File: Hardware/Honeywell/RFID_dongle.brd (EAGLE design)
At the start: 100 x 80 mm, 11 parts, among them J1 USB_B_PTH, J2 USB_A_PTH_MALE, J5 1X2-3.5MM, J6 1X2-3.5MM, Q1 35A/25V/8.5mΩ

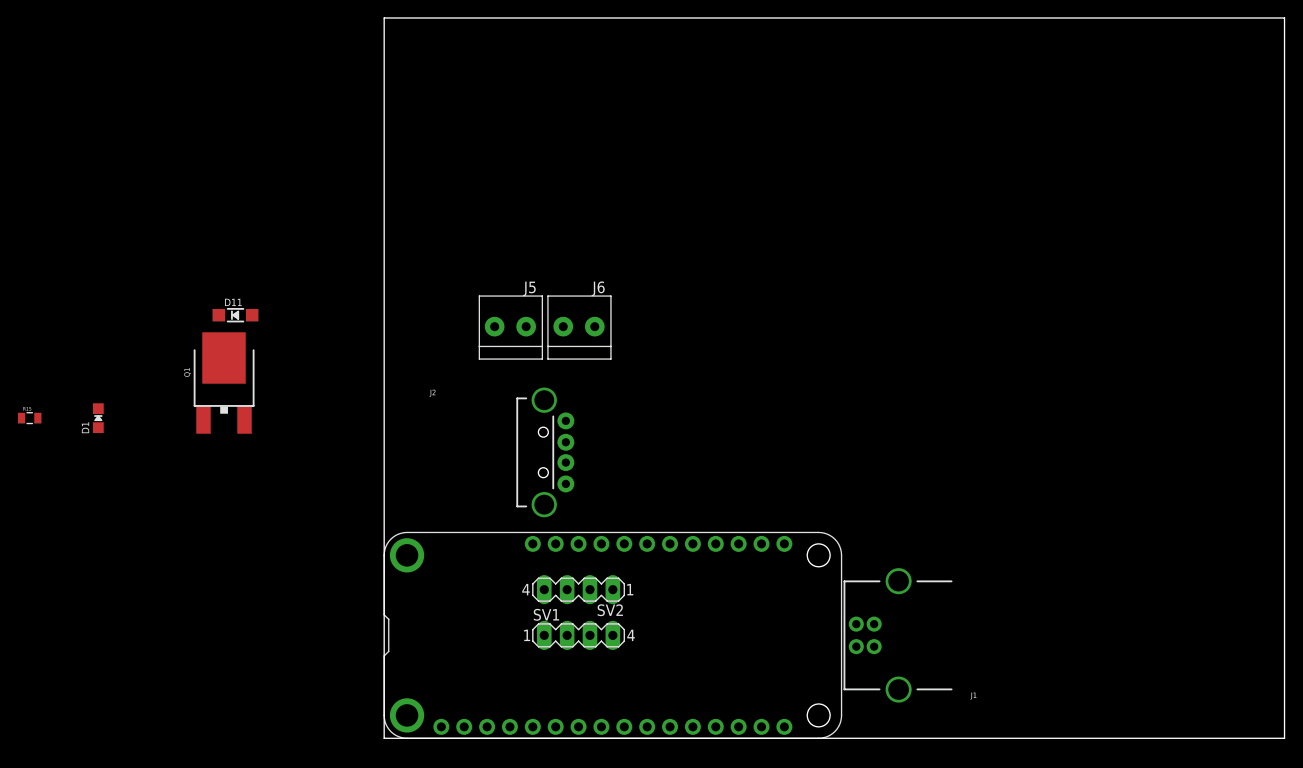
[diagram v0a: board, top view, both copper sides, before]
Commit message: HEEP-878 WIP, to be converted to USB switch IC
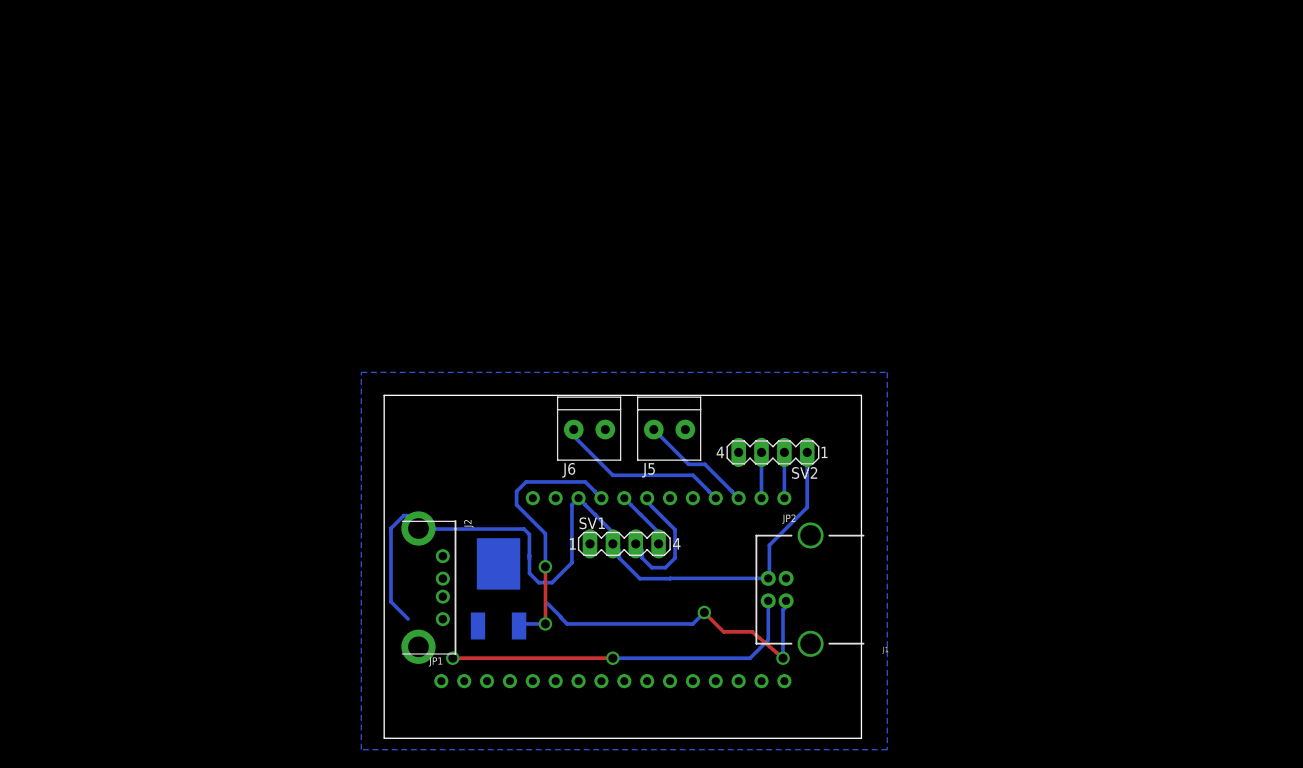
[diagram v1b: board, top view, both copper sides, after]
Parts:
- removed D1: (no value), microbuilder:CHIPLED_0805_NOOUTLINE
- removed D11: (no value), microbuilder:SOD-123
- removed MS1: FEATHERWING_NODIM, adafruit:FEATHERWING_DIM
- removed R15: 1K, SparkFun-Passives:0805
- added JP1: (no value), microbuilder:1X16_ROUND_MIN
- added JP2: (no value), microbuilder:1X12_ROUND_MIN
- J2: value USB_A_PTH_MALE -> (none); device SparkFun-Connectors:USB-A-H -> microbuilder:USB_HOST-PTH
- moved Q1 38.1 mm to (12.7, 17.8), flipped to the bottom
- moved SV2 26.4 mm to (43.2, 31.8)
- moved J2 23.3 mm to (0.00, 16.7), turned to 270 degrees
- moved J5 21.1 mm to (31.8, 34.3), turned to 180 degrees
- moved J6 11.5 mm to (22.9, 34.3), turned to 180 degrees
- moved SV1 11.4 mm to (26.7, 21.6)
- moved J1 11.0 mm to (48.6, 16.5)
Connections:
- removed net N$5: D1.C, R15.2
- removed net RX: SV1.3
- removed net TX: SV1.4
- new net RFID_RX: JP2.7, SV1.3
- new net RFID_TX: JP2.8, SV1.4
- net +5V: now also JP2.10; no longer D11.C
- net APA_CLK: now also JP2.2
- net APA_DATA: now also JP2.1
- net BUTT1: now also JP2.3
- net BUTT2: now also JP2.4
- net DRAIN1: no longer D11.A
- net EN1: now also JP2.9; no longer D1.A
- net GND: now also JP1.4; no longer MS1.4, R15.1
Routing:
- net +5V: track 0.00 -> 87.8 mm
- net N$2: track 0.00 -> 40.2 mm, vias 0 -> 2
- net N$6: track 0.00 -> 36.2 mm, vias 0 -> 2
- net EN1: track 0.00 -> 29.7 mm, vias 0 -> 2
- net BUTT2: track 0.00 -> 19.4 mm
- net RFID_RX: track 0.00 -> 14.3 mm
- net BUTT1: track 0.00 -> 12.6 mm
- net RFID_TX: track 0.00 -> 6.66 mm
- net APA_DATA: track 0.00 -> 5.08 mm
- net APA_CLK: track 0.00 -> 5.08 mm
- added copper zone on layer 16, net GND
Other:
- board size 100 x 80 mm -> 53 x 38.1 mm

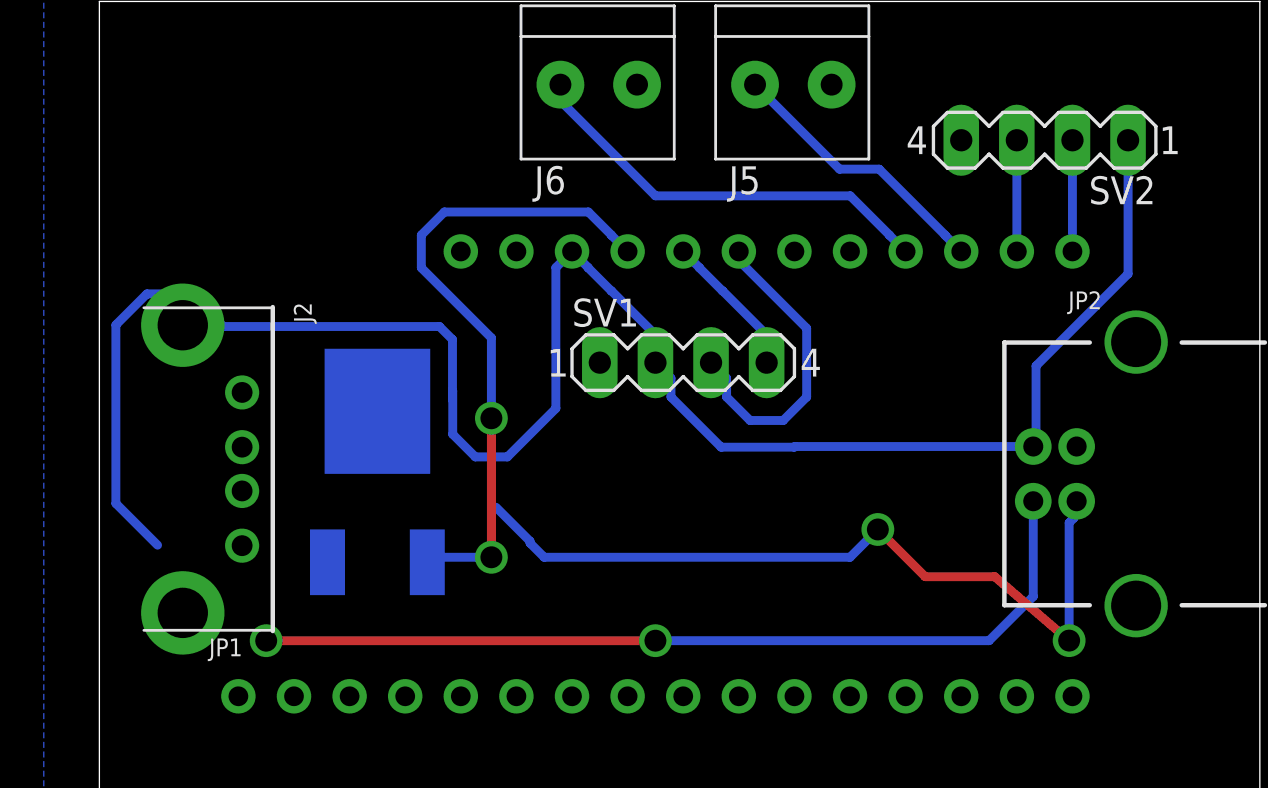
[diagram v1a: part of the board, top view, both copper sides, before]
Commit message: HEEP-878 working USB switch design, added USB switch IC to library
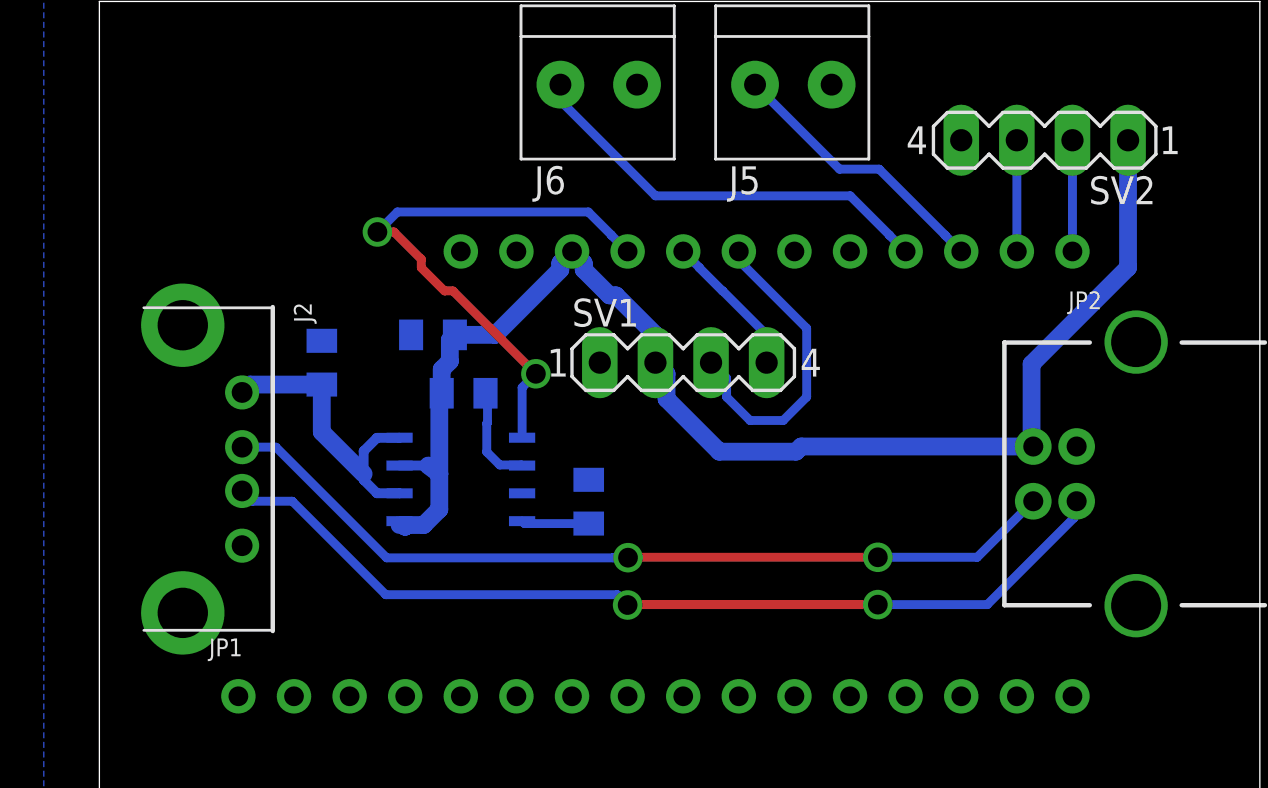
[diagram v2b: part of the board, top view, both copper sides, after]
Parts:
- removed Q1: 35A/25V/8.5mΩ, SparkFun-DiscreteSemi:DPAK
- added C1: 1uF, adafruit:C0805K
- added C2: 4.7uF, adafruit:C0805K
- added R1: 100K, adafruit:R0805
- added R2: 4.7K, adafruit:R0805
- added U1: 4MB Flash, Heep:SO08
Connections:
- removed net DRAIN1: J2.GND, Q1.4
- new net FAULT: R1.2, U1.2
- new net N$1: R2.1, U1.4
- new net USB_SWITCH: C2.2, J2.VBUS, U1.6, U1.8
- net +5V: now also C1.2, R1.1, U1.5, U1.7; no longer J2.VBUS
- net EN1: now also U1.1; no longer Q1.1
- net GND: now also C1.1, C2.1, J1.SHLD1, J1.SHLD2, J2.GND, J2.S1, J2.S2, R2.2, U1.3; no longer Q1.3
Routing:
- net +5V: track 87.8 -> 62.0 mm
- net USB_SWITCH: track 0.00 -> 13.8 mm
- net N$6: track 36.2 -> 42.6 mm
- net FAULT: track 0.00 -> 4.61 mm
- net EN1: track 29.7 -> 25.9 mm
- net N$1: track 0.00 -> 3.09 mm
- net N$2: track 40.2 -> 39.3 mm
